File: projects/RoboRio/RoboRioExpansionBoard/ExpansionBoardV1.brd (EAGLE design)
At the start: 96.2 x 80 mm, 92 parts, among them IC1 MC1525TO, Q1 5MHz

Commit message: minor changes
I tiptoe in ma jawdinz
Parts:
- moved U$4 2.66 mm to (95.7, 37.8)
- moved Q1 1.27 mm to (65.7, 39.4)
- flipped POWER3V3 to the top
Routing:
- net +3V3: track 270.0 -> 295.8 mm
- net !RESET: track 54.6 -> 52.1 mm
- net PWM8: track 27.9 -> 29.7 mm, vias 1 -> 0
- net N$2: track 5.67 -> 6.75 mm
- net +5V: track 157.7 -> 158.5 mm, vias 0 -> 3
- net IO14: vias 2 -> 1

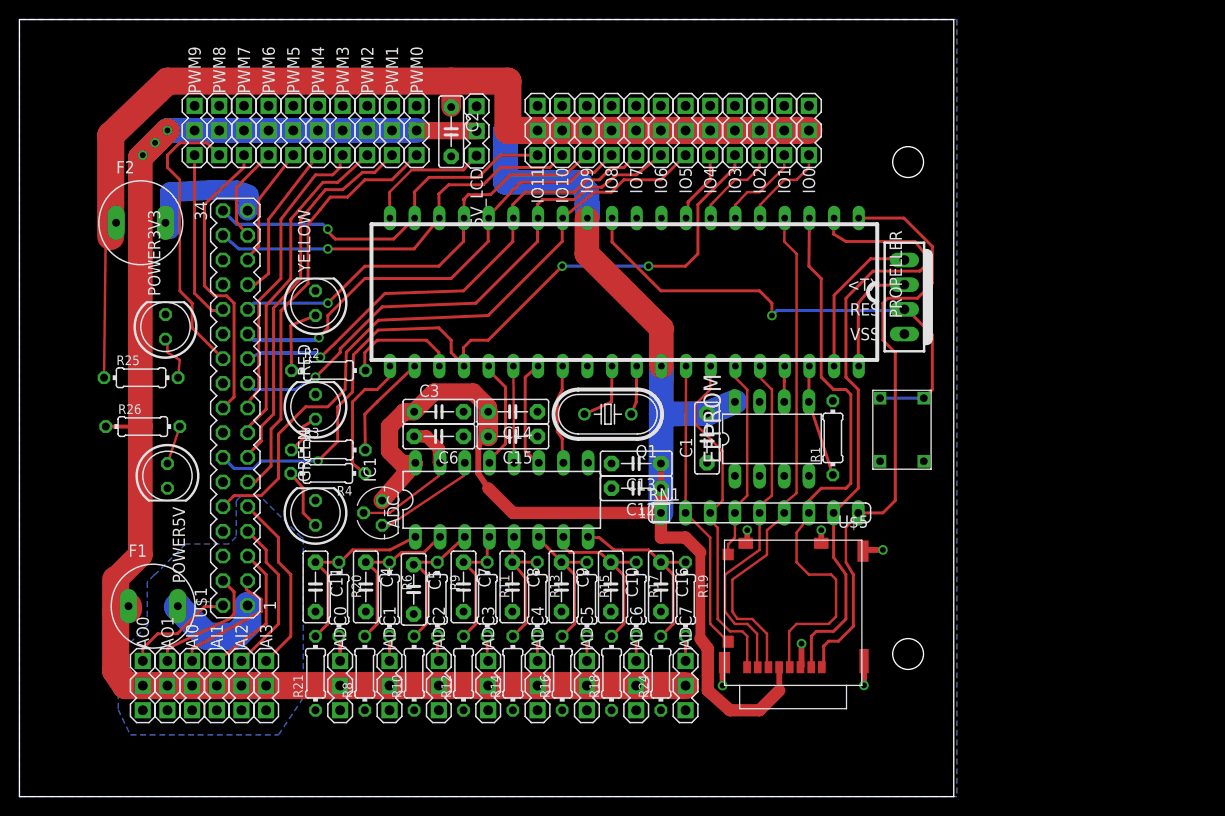
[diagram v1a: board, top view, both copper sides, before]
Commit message: Updated silkscreen markings, names of parts
and fixed small issue in microSD card
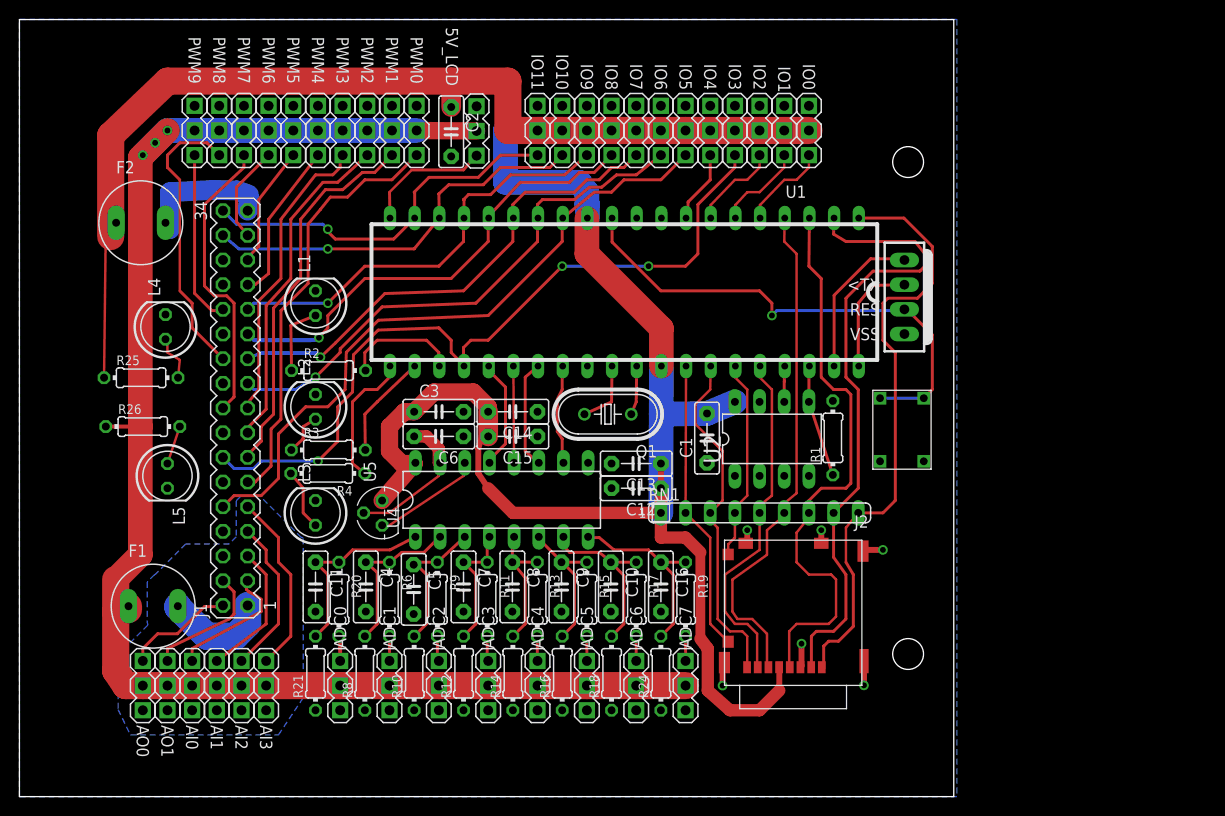
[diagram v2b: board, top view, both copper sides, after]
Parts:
- renumbered ADC to U4, EEPROM to U2, GREEN to L3, IC1 to U5, POWER3V3 to L4, POWER5V to L5, PROPELLER to U1, RED to L2, U$1 to J1, U$4 to U3, U$5 to J2, YELLOW to L1
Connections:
- net N$3 renamed L1

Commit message: Fixed most silkscreen errors
ADC inputs still need help.
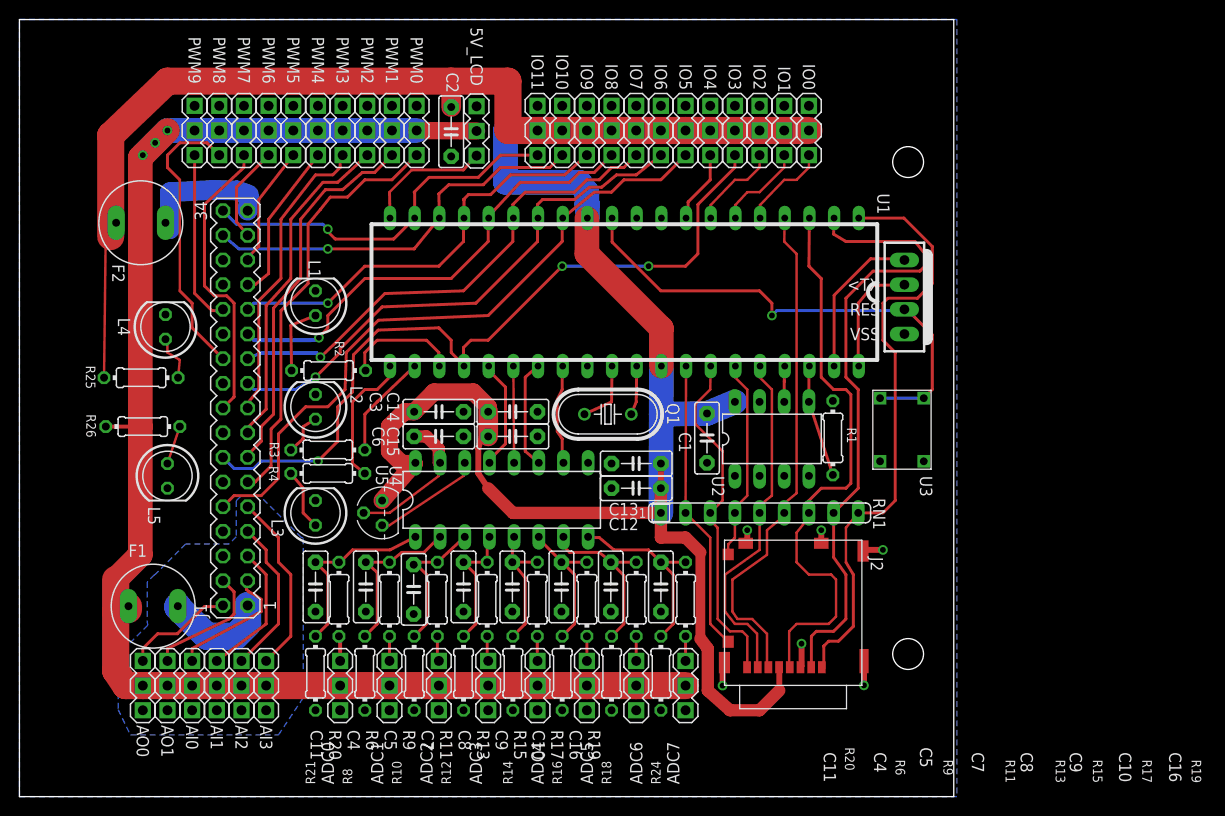
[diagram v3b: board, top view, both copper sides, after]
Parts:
- moved R3 0.05 mm to (36.8, 35.7)
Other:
- board text added: "R19 C16 R17 C10 R15 C9 R13 C8 R11 C7 R9 C5 R6 C4 R20 C11"
- board text added: "U3"

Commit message: Revert "Fixed most silkscreen errors"
This reverts commit 515101619b3595e4de045d44e07f2dfb83f59f1f.
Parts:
- moved R3 0.05 mm to (36.9, 35.7)
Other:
- board text removed: "R19 C16 R17 C10 R15 C9 R13 C8 R11 C7 R9 C5 R6 C4 R20 C11"
- board text removed: "U3"

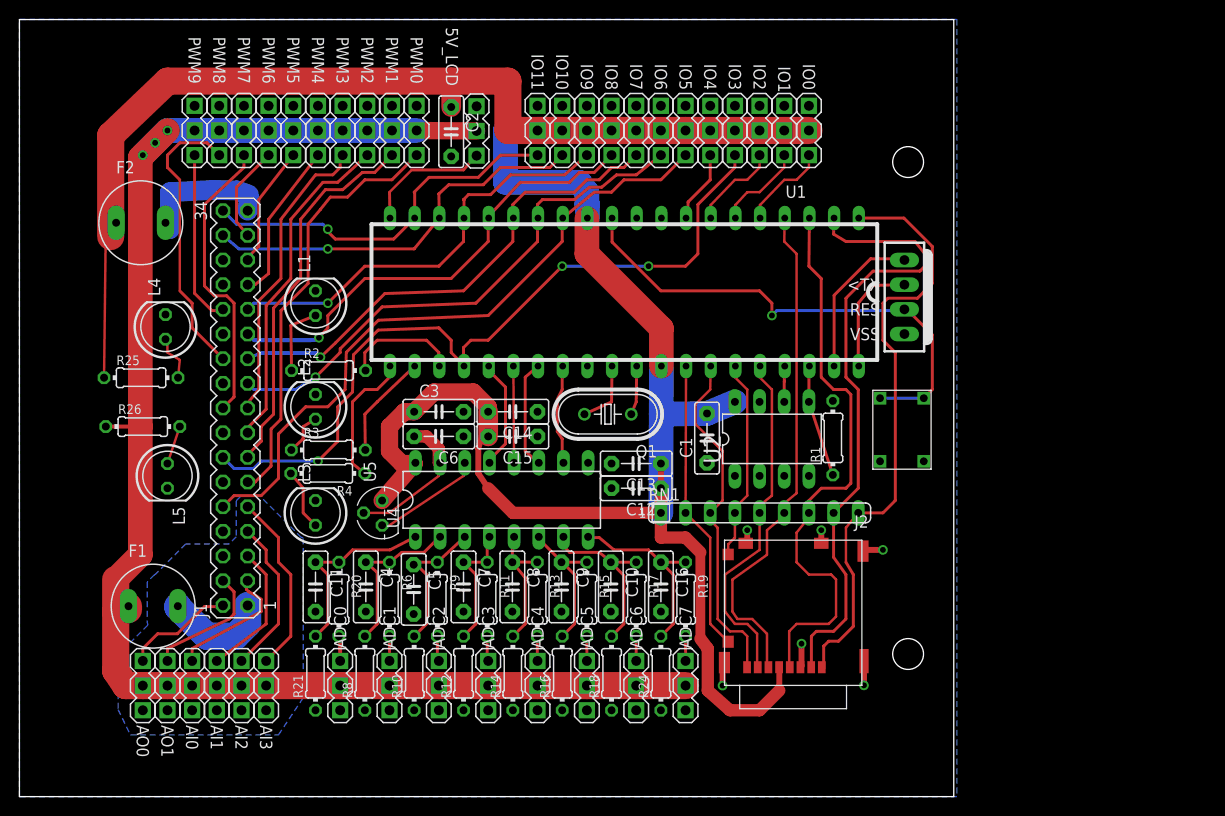
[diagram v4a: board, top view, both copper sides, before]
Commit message: Updated Silkscreen Layer
thanks to mr skeltin for reordered capacitor and resistor names.
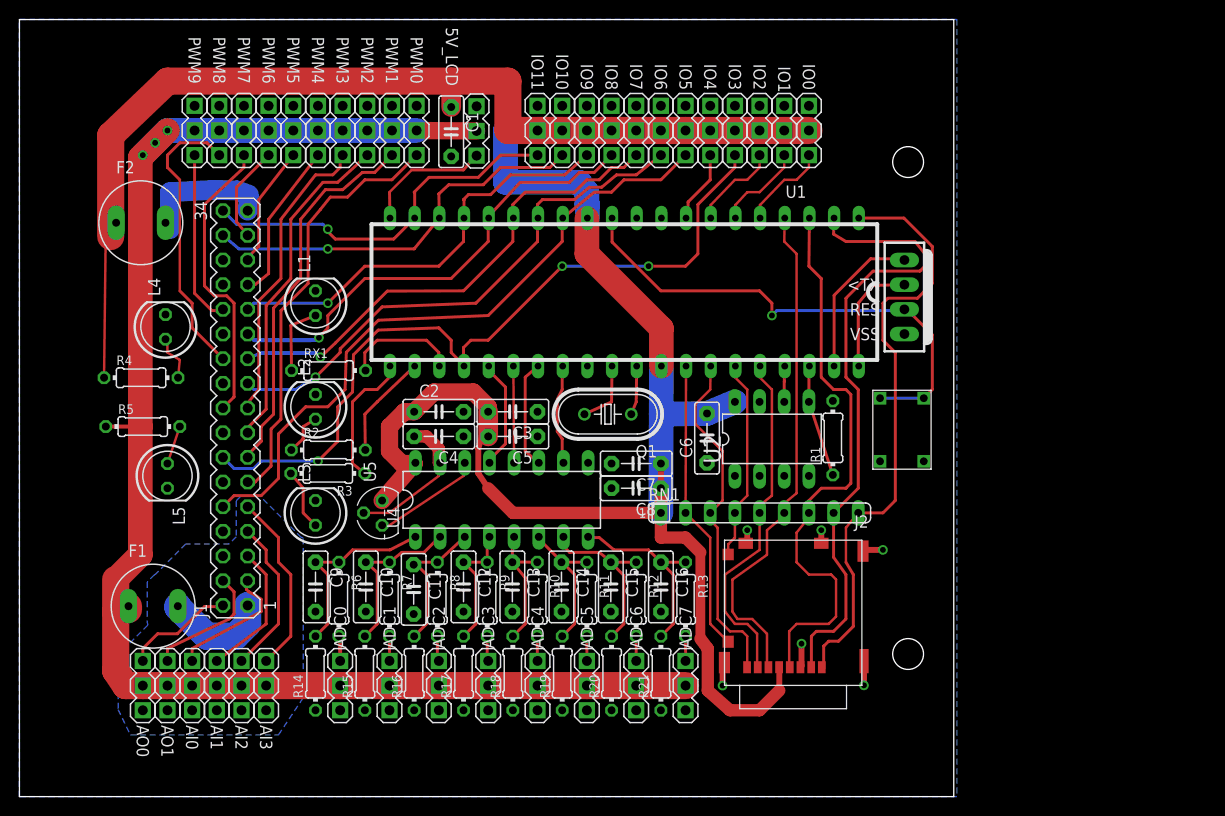
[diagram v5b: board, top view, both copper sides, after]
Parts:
- removed R24: 100, resistor:0204/7
- removed R25: 150, resistor:0204/7
- added R7: 100, resistor:0204/7
- added RX1: 150, resistor:0204/7
- C12, C14, C6: value 1uF -> .1uF
- C13, C15: value 10uF -> .1uF
- C3, C4, C8: value .1uF -> 1uF
- C5, C7: value .1uF -> 10uF
- moved C1 41.1 mm to (49.5, 68.5), turned to 270 degrees
- moved R21 35.6 mm to (71.1, 12.7)
- moved R20 29.1 mm to (66.0, 12.7), turned to 90 degrees
- moved C2 28.9 mm to (48.3, 39.6), turned to 0 degrees
- moved C6 27.6 mm to (75.9, 36.9), turned to 90 degrees
- moved C9 25.3 mm to (35.6, 21.6)
- moved C10 25.2 mm to (40.7, 21.6)
- moved R15 24.1 mm to (40.6, 12.7), turned to 90 degrees
- moved C7 21.8 mm to (68.6, 34.3), turned to 180 degrees
- moved R4 21.6 mm to (17.6, 43.1), turned to 0 degrees
- moved C12 20.5 mm to (50.8, 21.6), turned to 270 degrees
- moved R14 20.3 mm to (35.6, 12.7)
- moved R12 19.3 mm to (68.6, 20.3), turned to 270 degrees
- moved R17 19.3 mm to (50.8, 12.7), turned to 90 degrees
- moved C5 18.8 mm to (55.9, 37.1), turned to 180 degrees
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- renumbered R26 to R5
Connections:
- net +2V5: now also C4.2; no longer C6.2
- net +3V3: now also C1.1, C3.2, C5.2, C6.2, C7.1, C8.1, R4.1; no longer C1.2, C12.1, C13.1, C14.2, C15.2, C3.1, R25.1
- net DGND: now also C1.2, C14.2, C15.2, C3.1, C4.1, C5.1, R15.1, R17.1, R19.1, R20.1; no longer C1.1, C14.1, C15.1, C3.2, C4.2, C5.2, R10.1, R12.1, R24.1, R8.1
- net IO16: now also R3.1; no longer R4.1
- net IO17: now also R2.2; no longer R3.2
- net IO18: now also RX1.2; no longer R2.2
- net L1: now also R4.2; no longer R25.2
- net N$10: now also C12.1, R17.2, R9.1; no longer C7.1, R11.1, R12.2
- net N$12: now also R3.2; no longer R4.2
- net N$13: now also RX1.1; no longer R2.1
- net N$14: now also R2.1; no longer R3.1
- net N$16: now also C11.1, R16.2, R8.1; no longer C5.1, R10.2, R9.1
- net N$17: now also C13.1, R10.1, R18.2; no longer C8.1, R13.1, R14.2
- net N$22: now also R8.2; no longer R9.2
- net N$25: now also R9.2; no longer R11.2
- net N$29: now also R10.2; no longer R13.2
- net N$30: now also C14.1, R11.1, R19.2; no longer C9.1, R15.1, R16.2
- net N$31: now also R11.2; no longer R15.2
- net N$33: now also R6.2; no longer R20.2
- net N$34: now also R13.1, R21.2; no longer R19.1, R24.2
- net N$35: now also R12.2; no longer R17.2
- net N$36: now also R13.2; no longer R19.2
- net N$40: now also C15.1, R12.1, R20.2; no longer C10.1, R17.1, R18.2
- net N$7: now also R7.2; no longer R6.2
- net N$8: now also C9.1, R14.2, R6.1; no longer C11.1, R20.1, R21.2
- net N$9: now also C10.1, R15.2, R7.1; no longer C4.1, R6.1, R8.2

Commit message: Tidied up wires to be 45degrees
More need to be done, but most are finished.
The labels need to be done.
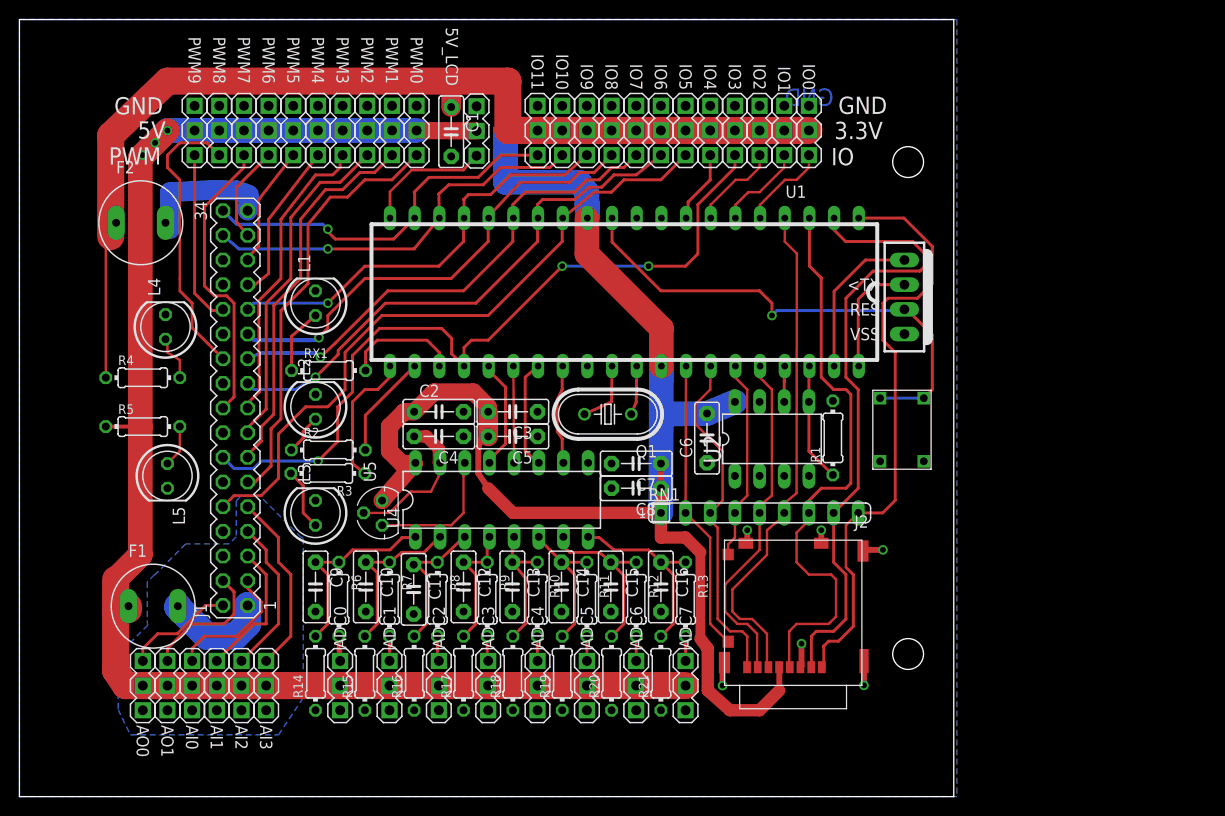
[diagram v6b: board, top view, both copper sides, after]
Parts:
- moved R4 0.18 mm to (17.8, 43.1)
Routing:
- net DGND: track 23.9 -> 26.7 mm
- net +2V5: track 15.0 -> 15.6 mm
- net SPECIAL29: track 11.6 -> 12.2 mm
- net N$13: track 7.38 -> 6.79 mm
- net AO1: track 12.9 -> 13.5 mm
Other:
- board text added: "3.3V"
- board text added: "5V"
- board text added: "GND"
- board text added: "IO"
- board text added: "PWM"

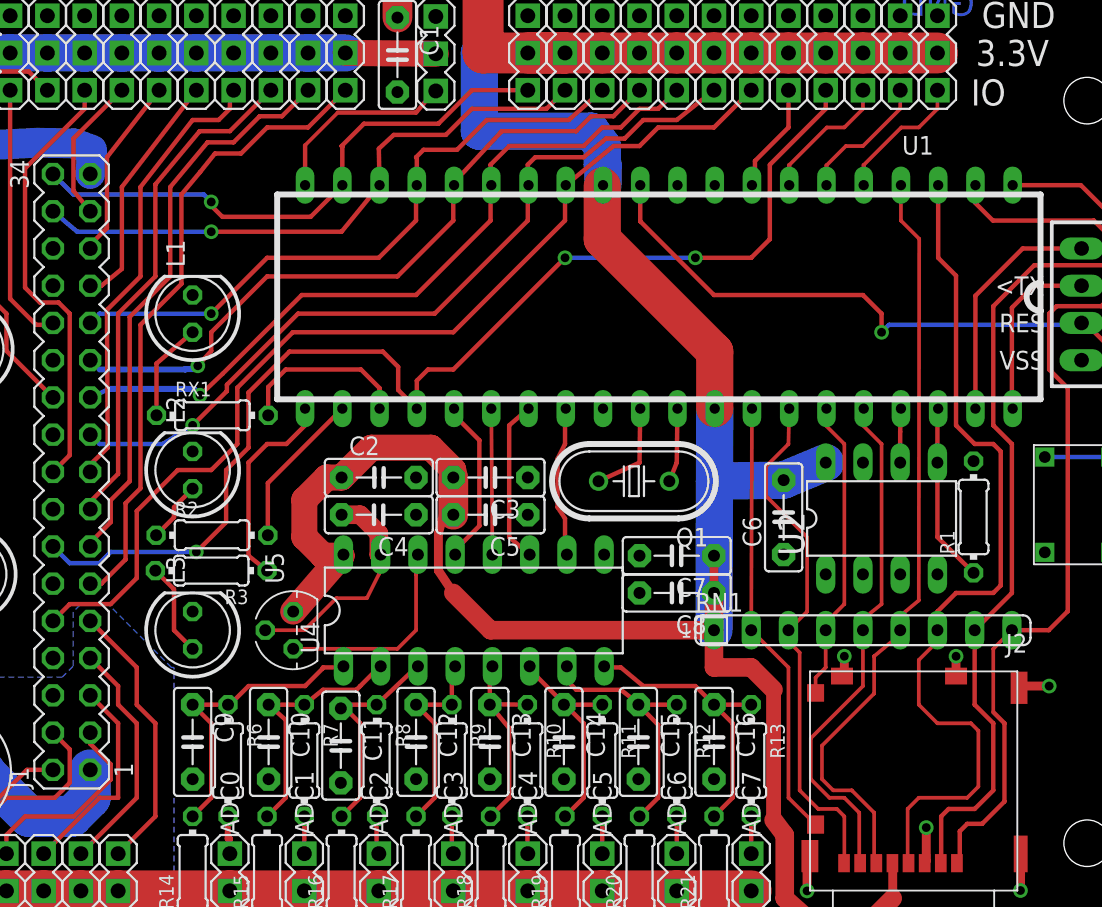
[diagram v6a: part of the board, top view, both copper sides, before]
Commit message: Fixed wires
in preparation for labels
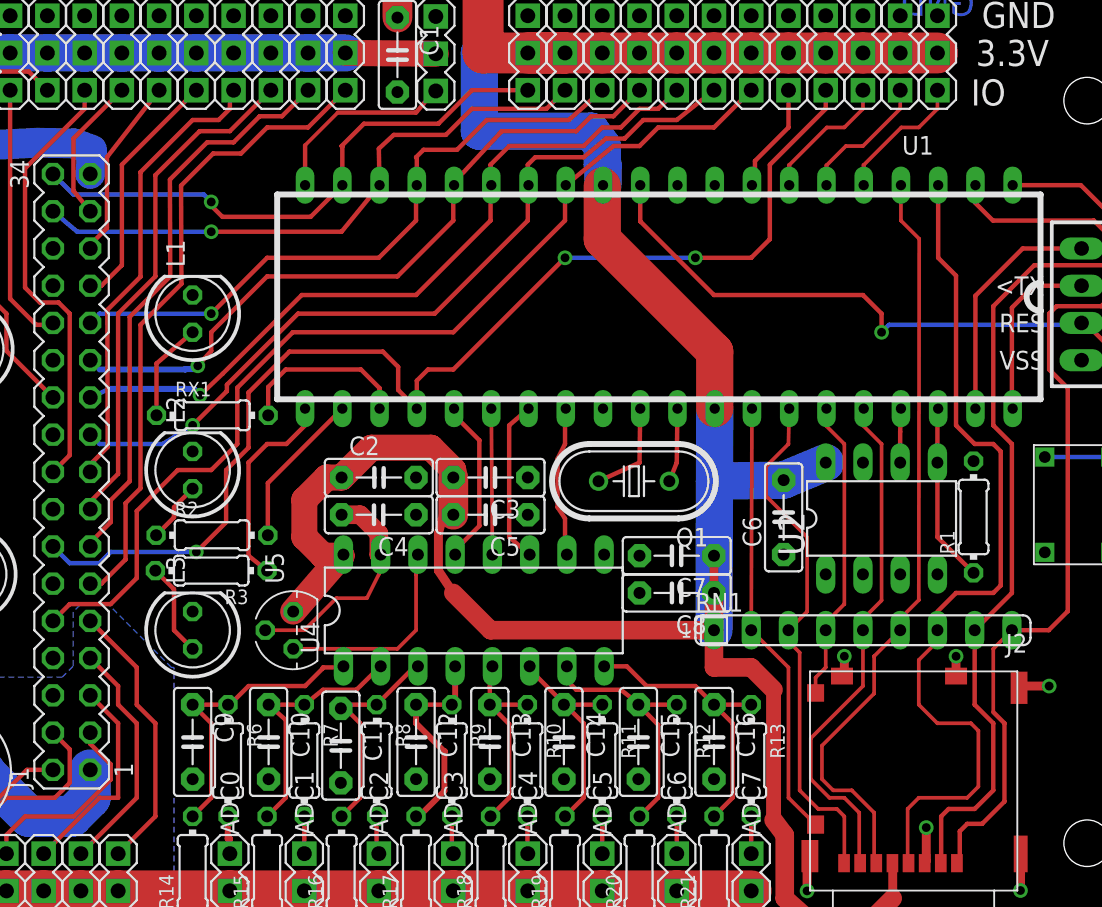
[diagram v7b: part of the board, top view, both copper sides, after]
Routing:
- net N$10: track 14.0 -> 14.7 mm
